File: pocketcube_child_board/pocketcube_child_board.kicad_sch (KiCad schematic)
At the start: 3 parts, among them J1 M55-7101242R

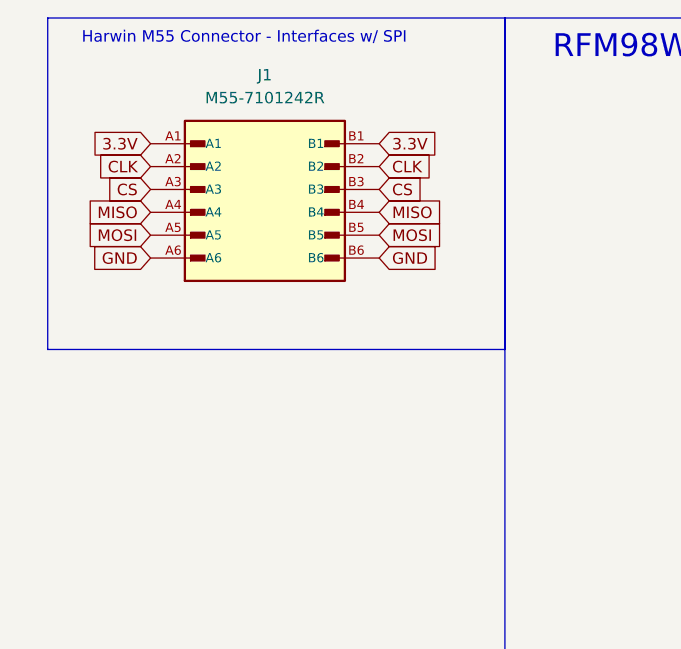
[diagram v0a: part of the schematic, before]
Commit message: Added new connector to PCB
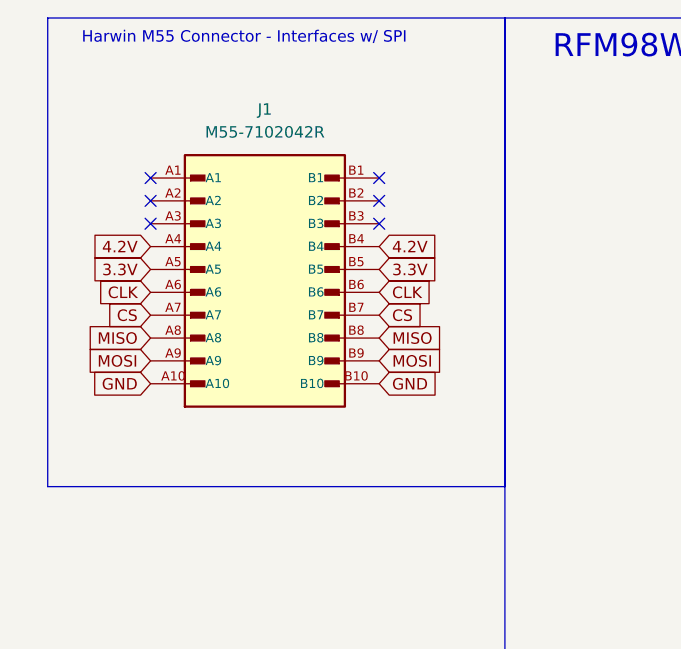
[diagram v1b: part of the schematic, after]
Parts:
- removed J1: M55-7101242R, inspirefly:HARWIN_M55-7101242R, symbol inspireFly:M55-7101242R
- added J1: M55-7102042R, inspirefly:HARWIN_M55-7102042R, symbol inspireFly:M55-7102042R
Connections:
- net 3.3V: now also J1.A5, J1.B5
- net CLK: now also J1.A6, J1.B6
- net CS: now also J1.A7, J1.B7
- net GND: now also J1.A10, J1.B10
- net MISO: now also J1.A8, J1.B8
- net MOSI: now also J1.A9, J1.B9
- new net 4.2V: J1.A4, J1.B4
- no-connect marks 12 -> 18

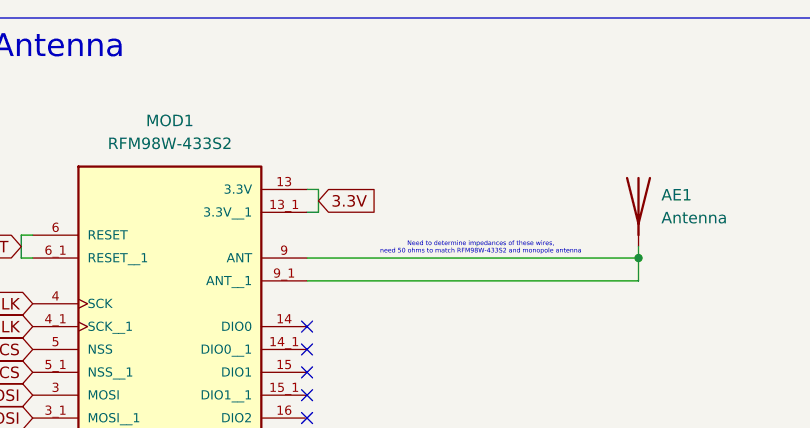
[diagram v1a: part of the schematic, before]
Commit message: Adding cap and finishing review
See teams message
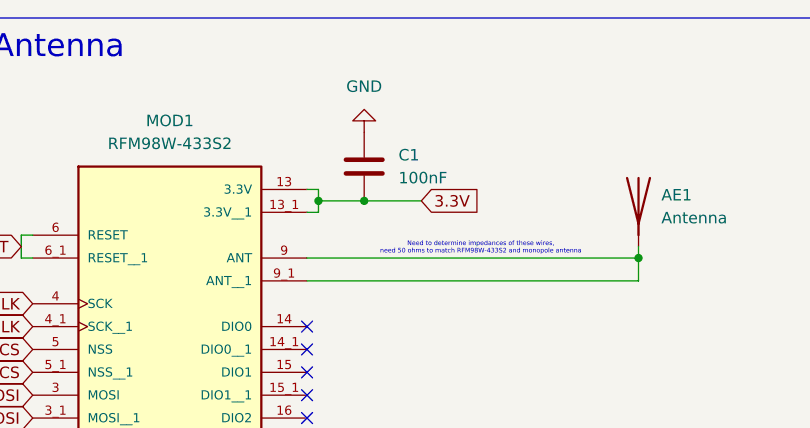
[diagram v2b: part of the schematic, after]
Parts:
- added C1: 100nF, Capacitor_SMD:C_0402_1005Metric_Pad0.74x0.62mm_HandSolder, symbol Device:C
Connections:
- net 3.3V: now also C1.2
- net GND: now also C1.1
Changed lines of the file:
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@@
+	)
+	(junction
+		(at 157.48 33.02)
+		(diameter 0)
+		(color 0 0 0 0)
 	)
 	(junction
@@
 	)
 	(junction
+		(at 162.56 33.02)
+		(diameter 0)
+		(color 0 0 0 0)
+	)
+	(junction
 		(at 166.37 92.71)
 		(diameter 0)
@@
 	(wire
 		(pts
+			(xy 168.91 33.02) (xy 162.56 33.02)
+		)
+		(stroke
+			(width 0)
+			(type default)
+		)
+	)
+	(wire
+		(pts
 			(xy 156.21 90.17) (xy 166.37 90.17)
 		)
@@
 	(wire
 		(pts
+			(xy 162.56 33.02) (xy 157.48 33.02)
+		)
+		(stroke
+			(width 0)
+			(type default)
+		)
+	)
+	(wire
+		(pts
 			(xy 166.37 85.09) (xy 166.37 87.63)
 		)
@@
 	(wire
 		(pts
+			(xy 157.48 33.02) (xy 157.48 34.29)
+		)
+		(stroke
+			(width 0)
+			(type default)
+		)
+	)
+	(wire
+		(pts
 			(xy 166.37 80.01) (xy 166.37 82.55)
 		)
@@
 	(wire
 		(pts
-			(xy 157.48 31.75) (xy 157.48 34.29)
+			(xy 157.48 31.75) (xy 157.48 33.02)
 		)
 		(stroke
@@
 	(global_label "3.3V"
 		(shape input)
-		(at 157.48 33.02 0)
+		(at 168.91 33.02 0)
 		(fields_autoplaced yes)
 		(effects
@@
 		)
 		(property "Intersheetrefs" "${INTERSHEET_REFS}"
-			(at 164.5776 33.02 0)
+			(at 176.0076 33.02 0)
 			(effects
 				(font
@@
 				(justify right)
 				(hide yes)
+			)
+		)
+	)
+	(symbol
+		(lib_id "Device:C")
+		(at 162.56 29.21 0)
+		(unit 1)
+		(exclude_from_sim no)
+		(in_bom yes)
+		(on_board yes)
+		(dnp no)
+		(fields_autoplaced yes)
+		(property "Reference" "C1"
+			(at 166.37 27.9399 0)
+			(effects
+				(font
+					(size 1.27 1.27)
+				)
+				(justify left)
+			)
+		)
+		(property "Value" "100nF"
+			(at 166.37 30.4799 0)
+			(effects
+				(font
+					(size 1.27 1.27)
+				)
+				(justify left)
+			)
+		)
+		(property "Footprint" "Capacitor_SMD:C_0402_1005Metric_Pad0.74x0.62mm_HandSolder"
+			(at 163.5252 33.02 0)
+			(effects
+				(font
+					(size 1.27 1.27)
+				)
+				(hide yes)
+			)
+		)
+		(property "Datasheet" "~"
+			(at 162.56 29.21 0)
+			(effects
+				(font
+					(size 1.27 1.27)
+				)
+				(hide yes)
+			)
+		)
+		(property "Description" "Unpolarized capacitor"
+			(at 162.56 29.21 0)
+			(effects
+				(font
+					(size 1.27 1.27)
+				)
+				(hide yes)
+			)
+		)
+		(pin "2"
+		)
+		(pin "1"
+		)
+		(instances
+			(project ""
+				(path "/a6e7c6fa-7853-41f6-bfd3-5d5ee6914f30"
+					(reference "C1")
+					(unit 1)
+				)
 			)
 		)
@@
 					(unit 1)
 				)
+			)
+		)
+	)
+	(symbol
+		(lib_id "power:GND")
+		(at 162.56 25.4 180)
+		(unit 1)
+		(exclude_from_sim no)
+		(in_bom yes)
+		(on_board yes)
+		(dnp no)
+		(fields_autoplaced yes)
+		(property "Reference" "#PWR02"
+			(at 162.56 19.05 0)
+			(effects
+				(font
+					(size 1.27 1.27)
+				)
+				(hide yes)
+			)
+		)
+		(property "Value" "GND"
+			(at 162.56 20.32 0)
+			(effects
+				(font
+					(size 1.27 1.27)
+				)
+			)
+		)
+		(property "Footprint" ""
+			(at 162.56 25.4 0)
+			(effects
+				(font
+					(size 1.27 1.27)
+				)
+				(hide yes)
+			)
+		)
+		(property "Datasheet" ""
+			(at 162.56 25.4 0)
+			(effects
+				(font
+					(size 1.27 1.27)
+				)
+				(hide yes)
+			)
+		)
+		(property "Description" "Power symbol creates a global label with name \"GND\" , ground"
+			(at 162.56 25.4 0)
+			(effects
+				(font
+					(size 1.27 1.27)
+				)
+				(hide yes)
+			)
+		)
+		(pin "1"
+		)
+		(instances
+			(project "pocketcube_child_board"
+				(path "/a6e7c6fa-7853-41f6-bfd3-5d5ee6914f30"
+					(reference "#PWR02")
+					(unit 1)
+				)

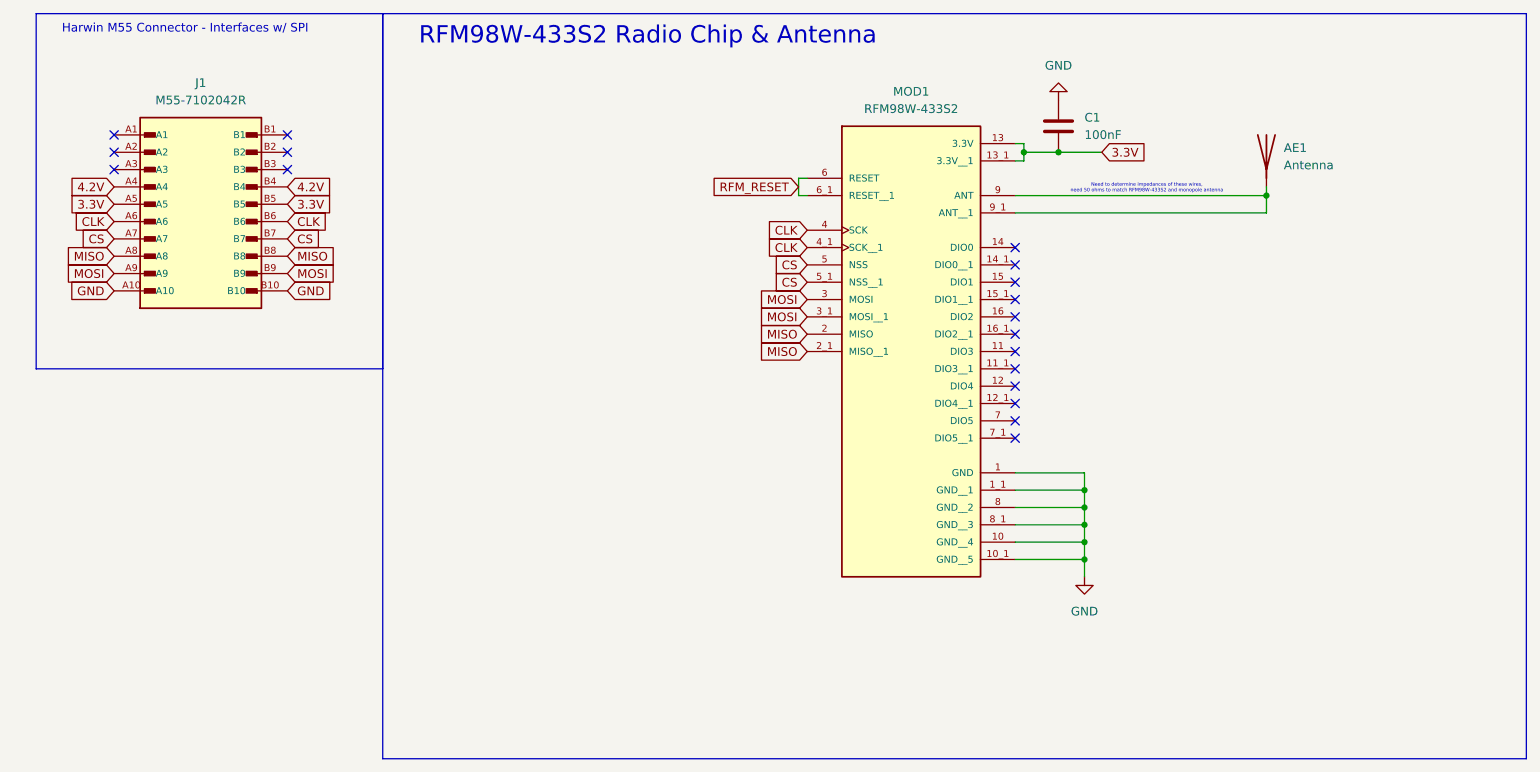
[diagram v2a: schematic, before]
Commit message: Edited PCB Layout & Rearranged Pins
I restructured the layout of the PCB due to traces going under the components, I also changed the pin order of the connector to add with routing
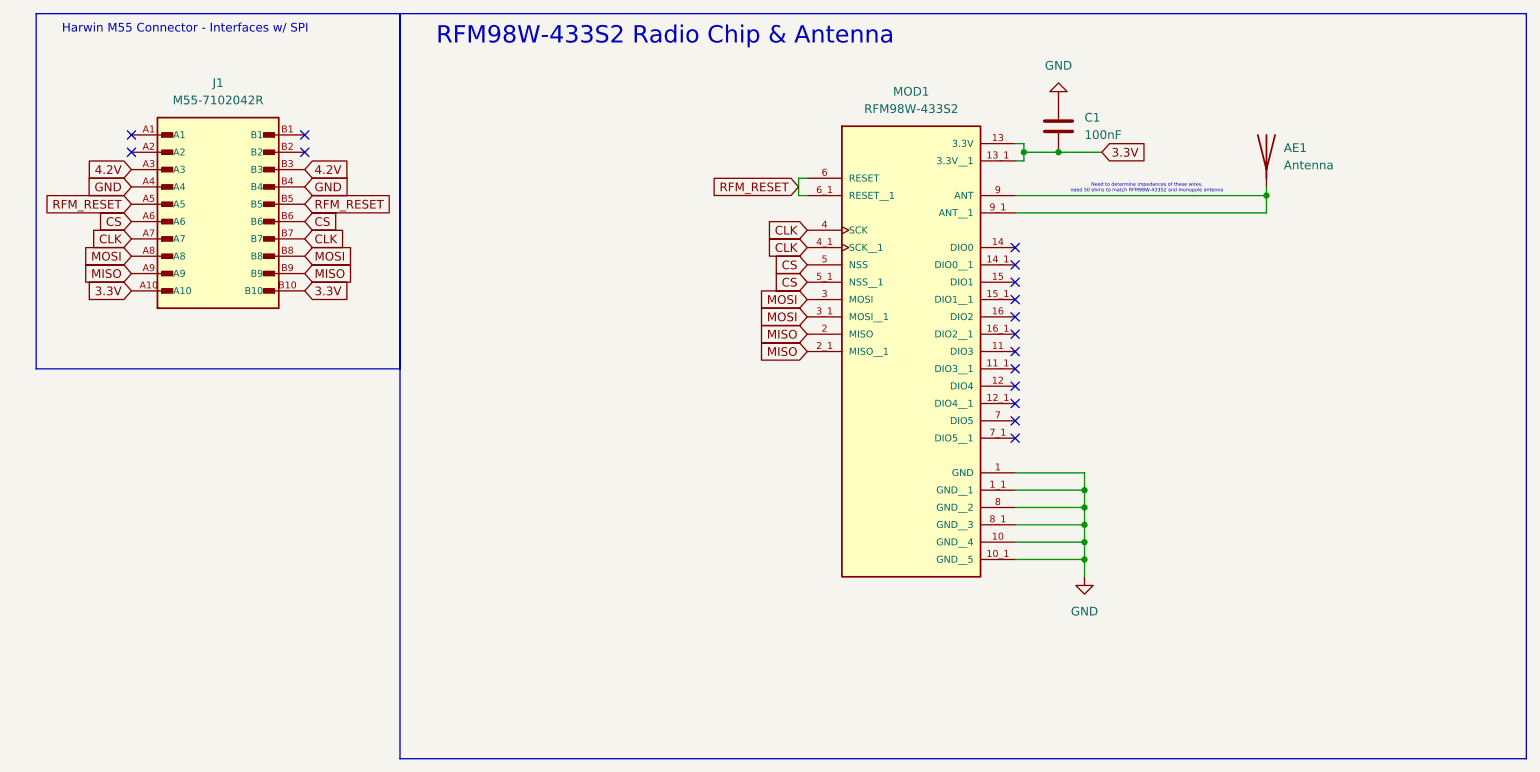
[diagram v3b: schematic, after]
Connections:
- net 3.3V: now also J1.A10, J1.B10; no longer J1.A5, J1.B5
- net 4.2V: now also J1.A3, J1.B3; no longer J1.A4, J1.B4
- net CLK: now also J1.A7, J1.B7; no longer J1.A6, J1.B6
- net CS: now also J1.A6, J1.B6; no longer J1.A7, J1.B7
- net GND: now also J1.A4, J1.B4; no longer J1.A10, J1.B10
- net MISO: now also J1.A9, J1.B9; no longer J1.A8, J1.B8
- net MOSI: now also J1.A8, J1.B8; no longer J1.A9, J1.B9
- net RFM_RESET: now also J1.A5, J1.B5
- no-connect marks 18 -> 16
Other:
- moved on the sheet: J1

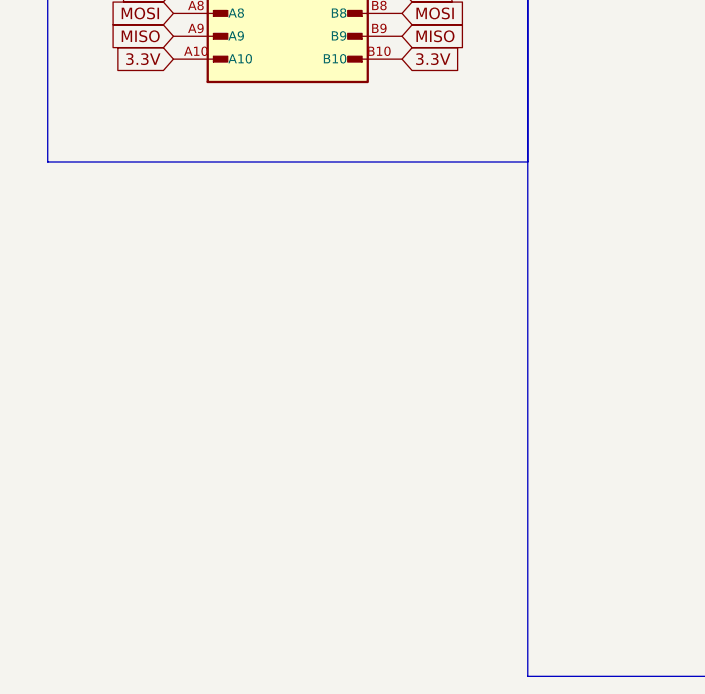
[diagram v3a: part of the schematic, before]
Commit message: Added SI3477DV-T1-GE3 P-Channel MOSFET to Schematic and PCB
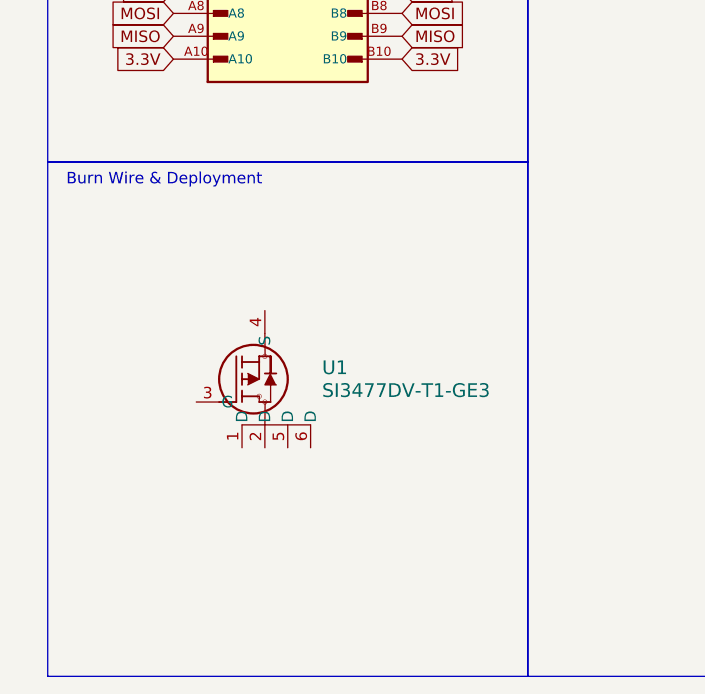
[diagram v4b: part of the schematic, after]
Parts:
- added U1: SI3477DV-T1-GE3, inspirefly:SOT_V-T1-GE3_VIS, symbol inspireFly:SI3477DV-T1-GE3
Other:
- note added: "Burn Wire & Deployment"
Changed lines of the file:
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@@
 	(paper "A4")
+	(rectangle
+		(start 12.7 64.77)
+		(end 66.04 121.92)
+		(stroke
+			(width 0)
+			(type default)
+		)
+		(fill
+			(type none)
+		)
+	)
 	(rectangle
 		(start 66.04 12.7)
@@
 		(fill
 			(type none)
+		)
+	)
+	(text "Burn Wire & Deployment"
+		(exclude_from_sim no)
+		(at 25.654 66.802 0)
+		(effects
+			(font
+				(size 1.27 1.27)
+			)
 		)
 	)
@@
 					(unit 1)
 				)
+			)
+		)
+	)
+	(symbol
+		(lib_id "inspireFly:SI3477DV-T1-GE3")
+		(at 29.21 91.44 0)
+		(unit 1)
+		(exclude_from_sim no)
+		(in_bom yes)
+		(on_board yes)
+		(dnp no)
+		(fields_autoplaced yes)
+		(property "Reference" "U1"
+			(at 43.18 87.6299 0)
+			(effects
+				(font
+					(size 1.524 1.524)
+				)
+				(justify left)
+			)
+		)
+		(property "Value" "SI3477DV-T1-GE3"
+			(at 43.18 90.1699 0)
+			(effects
+				(font
+					(size 1.524 1.524)
+				)
+				(justify left)
+			)
+		)
+		(property "Footprint" "inspirefly:SOT_V-T1-GE3_VIS"
+			(at 29.21 91.44 0)
+			(effects
+				(font
+					(size 1.27 1.27)
+					(italic yes)
+				)
+				(hide yes)
+			)
+		)
+		(property "Datasheet" "https://www.vishay.com/doc?70865"
+			(at 29.21 91.44 0)
+			(effects
+				(font
+					(size 1.27 1.27)
+					(italic yes)
+				)
+				(hide yes)
+			)
+		)
+		(property "Description" ""
+			(at 29.21 91.44 0)
+			(effects
+				(font
+					(size 1.27 1.27)
+				)
+				(hide yes)
+			)
+		)
+		(pin "5"
+		)
+		(pin "1"
+		)
+		(pin "6"
+		)
+		(pin "3"
+		)
+		(pin "2"
+		)
+		(pin "4"
+		)
+		(instances
+			(project ""
+				(path "/a6e7c6fa-7853-41f6-bfd3-5d5ee6914f30"
+					(reference "U1")
+					(unit 1)
+				)

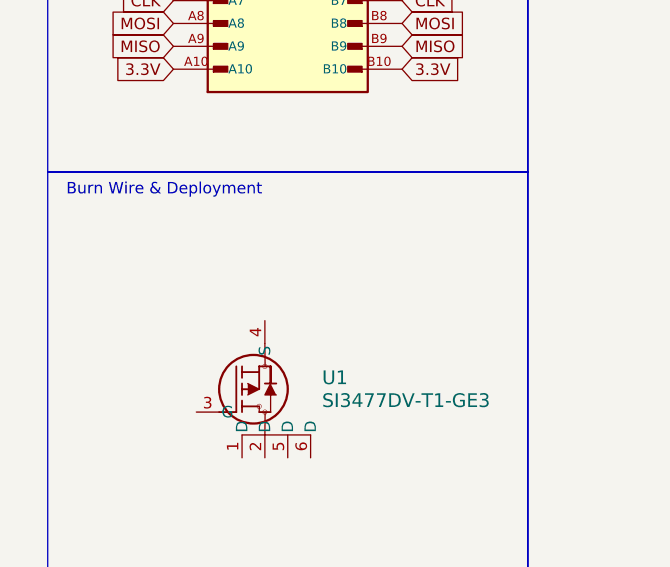
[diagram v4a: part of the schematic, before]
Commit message: Integrating P-Channel MOSFET
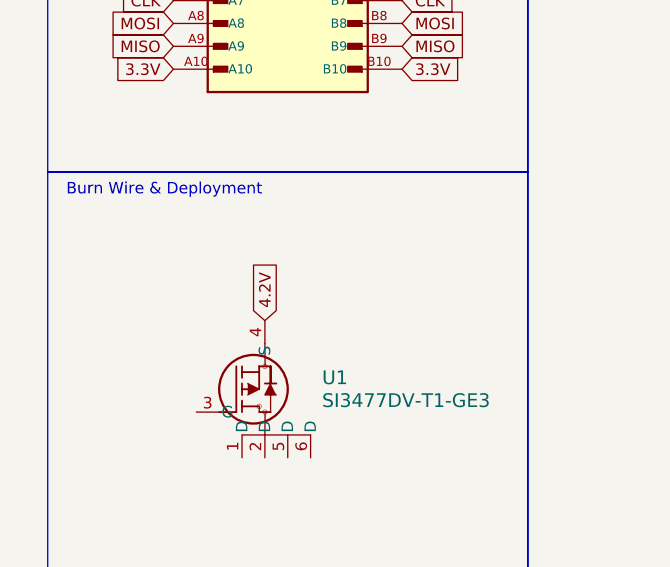
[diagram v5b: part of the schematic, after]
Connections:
- net 4.2V: now also U1.4 (S)
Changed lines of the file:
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@@
+		)
+	)
+	(global_label "4.2V"
+		(shape input)
+		(at 36.83 81.28 90)
+		(fields_autoplaced yes)
+		(effects
+			(font
+				(size 1.27 1.27)
+			)
+			(justify left)
+		)
+		(property "Intersheetrefs" "${INTERSHEET_REFS}"
+			(at 36.83 74.1824 90)
+			(effects
+				(font
+					(size 1.27 1.27)
+				)
+				(justify left)
+				(hide yes)
+			)
 		)
 	)
